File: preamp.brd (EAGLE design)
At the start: 100 x 80 mm, 70 parts, among them IC1 INA217DW, IC2 OPA134U, IC3 PCM1808, IC4 12.288MHz, IC5 REG1117

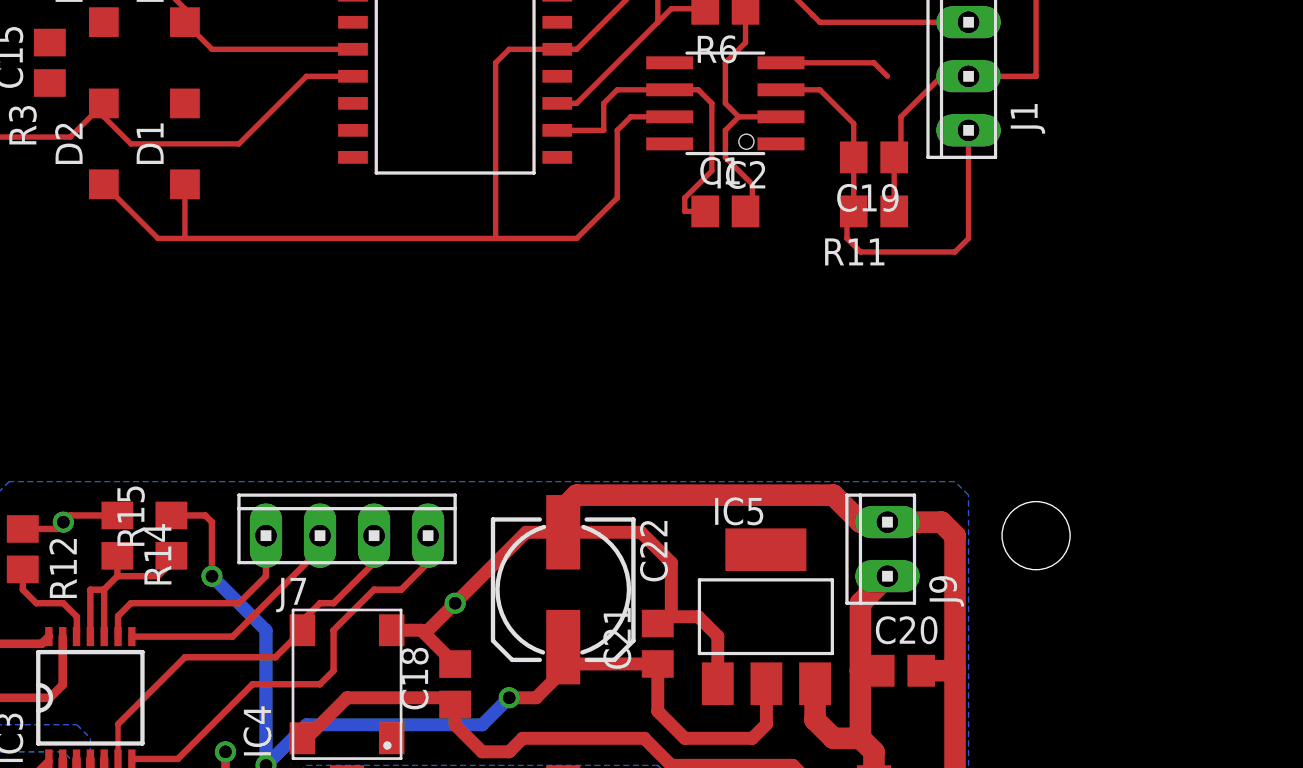
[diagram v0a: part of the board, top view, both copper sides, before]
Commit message: after review: named wires, add divider to ref voltage, add GND to digital pins
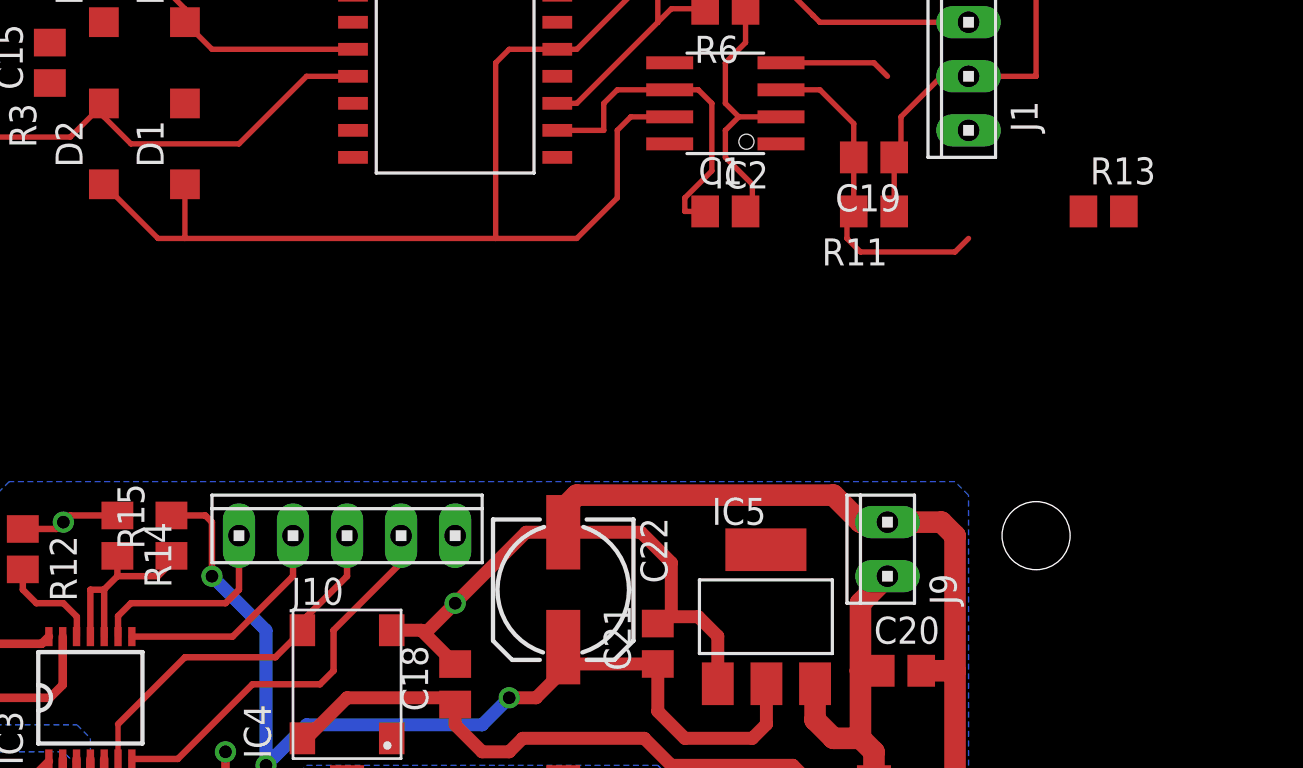
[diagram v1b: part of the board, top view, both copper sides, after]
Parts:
- removed J7: (no value), con-amp:10X04MTA
- added J10: (no value), con-amp:10X05MTA
- added R13: 0, rcl:R0805
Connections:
- new net N$28: J1.3, R13.2
- net GND: now also J10.1
- net N$15: now also R13.1; no longer J1.3
- net N$18: now also J10.2; no longer J7.1
- net N$19: now also J10.4; no longer J7.3
- net N$8: now also J10.3; no longer J7.2
- net N$9: now also J10.5; no longer J7.4
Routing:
- net N$15: track 20.9 -> 15.8 mm
- net N$18: track 20.1 -> 18.9 mm
- net N$9: track 10.6 -> 9.70 mm
- net N$8: track 18.8 -> 17.9 mm
- net N$19: track 11.2 -> 10.7 mm
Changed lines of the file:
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@@
 <element name="IC4" library="rpiadc" package="KXO-97" value="12.288MHz" x="40.005" y="14.605" rot="R90"/>
 <element name="C18" library="rcl" package="C0805" value="0.1" x="45.085" y="14.605" rot="R90"/>
-<element name="J7" library="con-amp" package="10X04MTA" value="" x="40.005" y="21.59"/>
 <element name="C19" library="rcl" package="C0805" value="0.1" x="64.77" y="39.37" rot="R180"/>
 <element name="R12" library="rcl" package="R0805" value="1k" x="24.765" y="20.955" rot="R270"/>
@@
 <element name="C31" library="rcl" package="153CLV-0605" value="47" x="40.005" y="6.35" rot="R90"/>
 <element name="R17" library="rcl" package="R0805" value="0" x="59.055" y="3.175"/>
+<element name="R13" library="rcl" package="R0805" value="0" x="75.565" y="36.83"/>
+<element name="J10" library="con-amp" package="10X05MTA" value="" x="40.005" y="21.59"/>
 </elements>
 <signals>
@@
 <contactref element="R11" pad="2"/>
 <contactref element="C19" pad="2"/>
-<contactref element="J1" pad="3"/>
-<wire x1="69.215" y1="40.64" x2="69.215" y2="35.56" width="0.254" layer="1"/>
 <wire x1="69.215" y1="35.56" x2="68.58" y2="34.925" width="0.254" layer="1"/>
 <wire x1="68.58" y1="34.925" x2="64.135" y2="34.925" width="0.254" layer="1"/>
@@
 <wire x1="63.82" y1="40.955" x2="62.23" y2="42.545" width="0.254" layer="1"/>
 <wire x1="62.23" y1="42.545" x2="60.4012" y2="42.545" width="0.254" layer="1"/>
+<contactref element="R13" pad="1"/>
+<wire x1="69.215" y1="35.56" x2="74.615" y2="36.83" width="0" layer="19" extent="1-1"/>
 </signal>
 <signal name="N$8">
@@
 <wire x1="29.24" y1="11.095" x2="29.24" y2="12.73" width="0.254" layer="1"/>
 <wire x1="37.905" y1="17.145" x2="37.905" y2="17.585" width="0.3048" layer="1"/>
-<contactref element="J7" pad="2"/>
 <wire x1="38.1" y1="17.78" x2="38.1" y2="17.34" width="0.3048" layer="1"/>
 <wire x1="38.1" y1="17.34" x2="37.905" y2="17.145" width="0.3048" layer="1"/>
@@
 <wire x1="32.385" y1="15.875" x2="36.635" y2="15.875" width="0.3048" layer="1"/>
 <wire x1="36.635" y1="15.875" x2="37.905" y2="17.145" width="0.3048" layer="1"/>
-<wire x1="41.275" y1="21.59" x2="41.275" y2="20.32" width="0.3048" layer="1"/>
-<wire x1="38.735" y1="18.415" x2="38.1" y2="17.78" width="0.3048" layer="1"/>
-<wire x1="38.735" y1="18.415" x2="39.37" y2="18.415" width="0.3048" layer="1"/>
-<wire x1="39.37" y1="18.415" x2="41.275" y2="20.32" width="0.3048" layer="1"/>
+<contactref element="J10" pad="3"/>
+<wire x1="38.1" y1="17.78" x2="40.005" y2="19.685" width="0.3048" layer="1"/>
+<wire x1="40.005" y1="19.685" x2="40.005" y2="21.59" width="0.3048" layer="1"/>
 </signal>
 <signal name="N$9">
@@
 <wire x1="29.24" y1="16.845" x2="29.24" y2="17.81" width="0.3048" layer="1"/>
 <wire x1="29.24" y1="17.81" x2="29.845" y2="18.415" width="0.3048" layer="1"/>
-<wire x1="29.845" y1="18.415" x2="34.925" y2="18.415" width="0.3048" layer="1"/>
-<contactref element="J7" pad="4"/>
-<wire x1="34.925" y1="18.415" x2="36.195" y2="19.685" width="0.3048" layer="1"/>
-<wire x1="36.195" y1="19.685" x2="36.195" y2="21.59" width="0.3048" layer="1"/>
+<contactref element="J10" pad="5"/>
+<wire x1="29.845" y1="18.415" x2="34.29" y2="18.415" width="0.3048" layer="1"/>
+<wire x1="34.29" y1="18.415" x2="34.925" y2="19.05" width="0.3048" layer="1"/>
+<wire x1="34.925" y1="19.05" x2="34.925" y2="21.59" width="0.3048" layer="1"/>
 </signal>
 <signal name="N$22">
@@
 <wire x1="50.8" y1="23.495" x2="50.165" y2="22.86" width="1.016" layer="1"/>
 <wire x1="50.165" y1="22.86" x2="50.165" y2="21.59" width="1.016" layer="1"/>
+<contactref element="J10" pad="1"/>
 <wire x1="11.11" y1="73.025" x2="10.795" y2="76.835" width="0" layer="19" extent="1-1"/>
 <wire x1="8.03" y1="67.865" x2="11.11" y2="73.025" width="0" layer="19" extent="1-1"/>
@@
 </signal>
 <signal name="N$18">
-<contactref element="J7" pad="1"/>
 <contactref element="IC3" pad="7"/>
 <wire x1="29.89" y1="11.095" x2="32.05" y2="11.095" width="0.3048" layer="1"/>
@@
 <wire x1="35.56" y1="14.605" x2="38.735" y2="14.605" width="0.3048" layer="1"/>
 <wire x1="38.735" y1="14.605" x2="39.37" y2="15.24" width="0.3048" layer="1"/>
-<wire x1="43.815" y1="21.59" x2="43.815" y2="20.32" width="0.3048" layer="1"/>
-<wire x1="43.815" y1="20.32" x2="42.545" y2="19.05" width="0.3048" layer="1"/>
-<wire x1="42.545" y1="19.05" x2="41.275" y2="19.05" width="0.3048" layer="1"/>
-<wire x1="41.275" y1="19.05" x2="39.37" y2="17.145" width="0.3048" layer="1"/>
+<wire x1="42.545" y1="20.32" x2="39.37" y2="17.145" width="0.3048" layer="1"/>
 <wire x1="39.37" y1="17.145" x2="39.37" y2="15.24" width="0.3048" layer="1"/>
+<contactref element="J10" pad="2"/>
+<wire x1="42.545" y1="20.32" x2="42.545" y2="21.59" width="0.3048" layer="1"/>
 </signal>
 <signal name="N$19">
 <contactref element="IC3" pad="8"/>
-<contactref element="J7" pad="3"/>
 <wire x1="29.89" y1="16.845" x2="34.625" y2="16.845" width="0.3048" layer="1"/>
-<wire x1="38.735" y1="21.59" x2="38.735" y2="20.955" width="0.3048" layer="1"/>
-<wire x1="38.735" y1="20.955" x2="34.625" y2="16.845" width="0.3048" layer="1"/>
+<contactref element="J10" pad="4"/>
+<wire x1="34.625" y1="16.845" x2="37.465" y2="19.685" width="0.3048" layer="1"/>
+<wire x1="37.465" y1="19.685" x2="37.465" y2="21.59" width="0.3048" layer="1"/>
 </signal>
 <signal name="N$26">
@@
 </polygon>
 </signal>
+<signal name="N$28">
+<contactref element="J1" pad="3"/>
+<contactref element="R13" pad="2"/>
+<wire x1="69.215" y1="40.64" x2="76.515" y2="36.83" width="0" layer="19" extent="1-1"/>
+</signal>
 </signals>

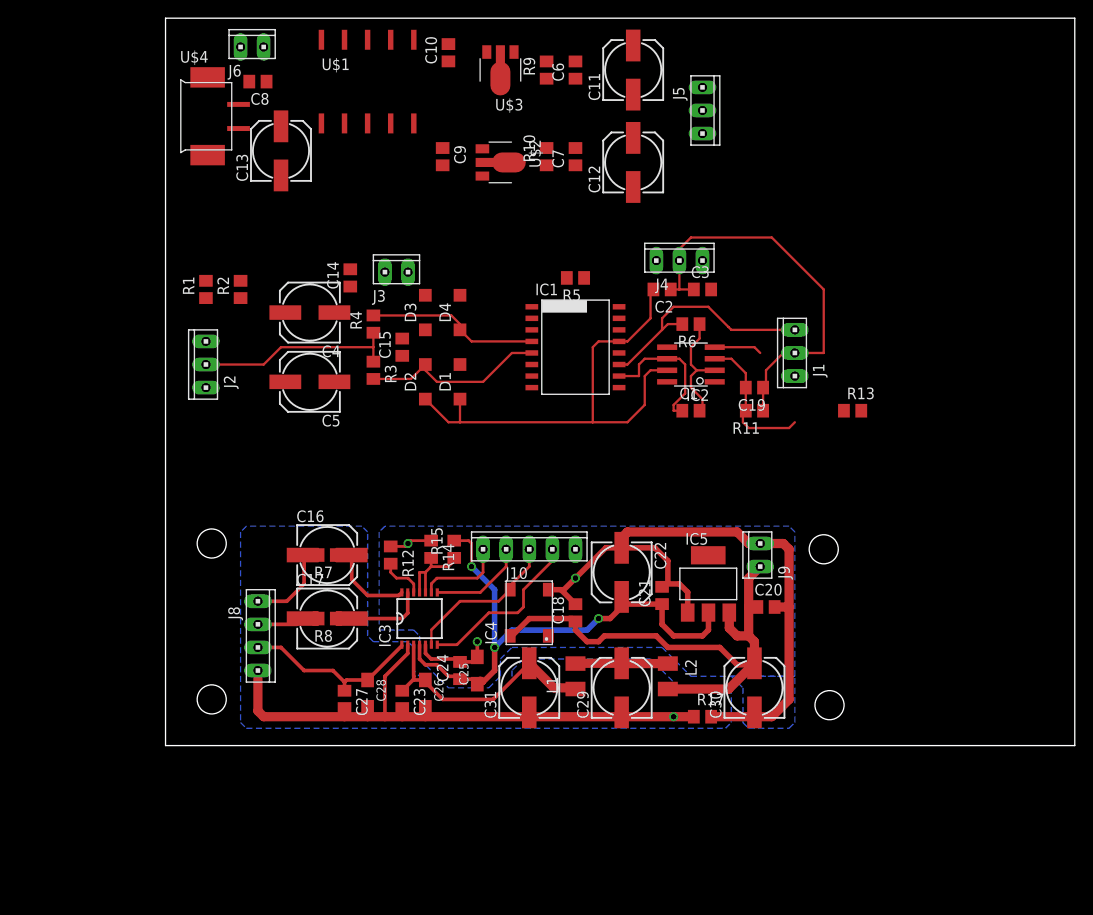
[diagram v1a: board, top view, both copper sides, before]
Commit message: route preamp, check DRC 0.254 mm
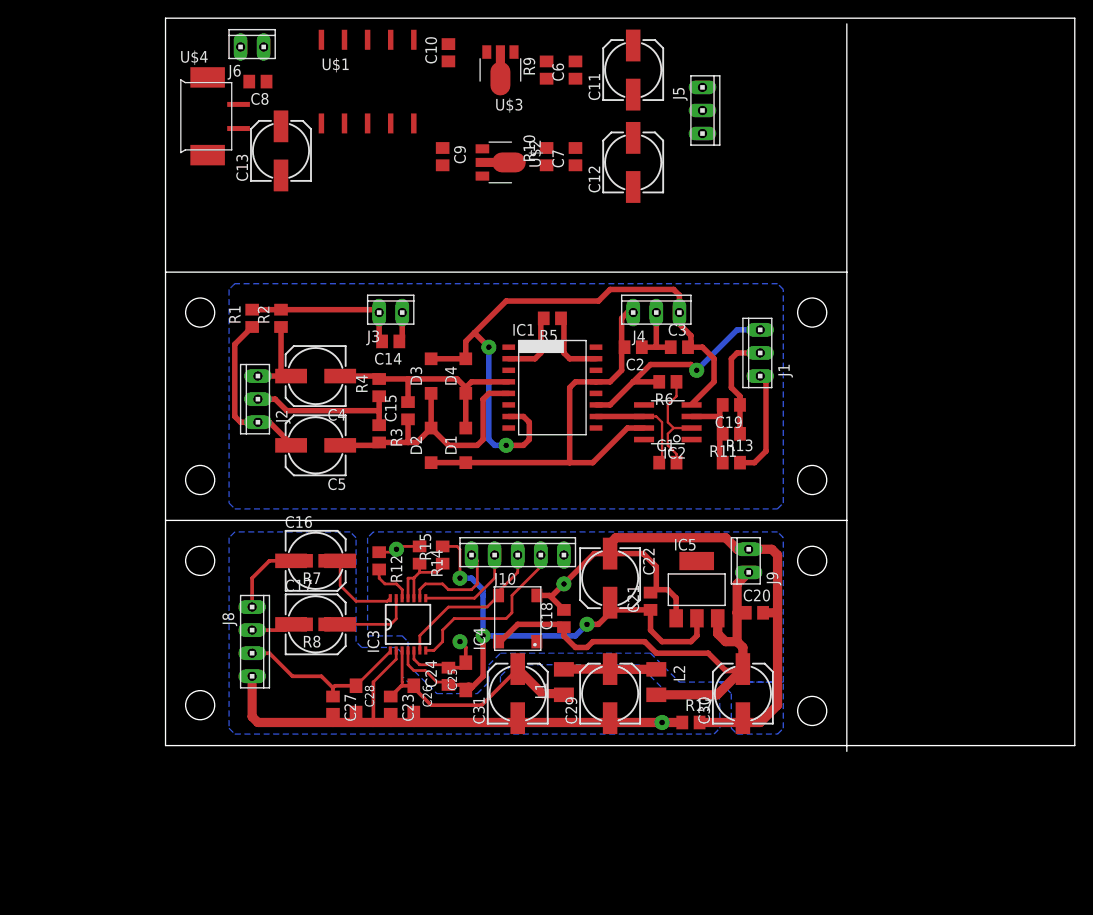
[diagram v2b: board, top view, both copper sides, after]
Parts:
- moved R13 14.5 mm to (62.2, 31.1)
- moved C14 8.28 mm to (24.8, 44.5), turned to 180 degrees
- moved C2 7.10 mm to (51.4, 43.8)
- moved C15 7.01 mm to (26.7, 36.8)
- moved C4 7.01 mm to (16.5, 40.6)
- moved C5 7.01 mm to (16.5, 33.0)
- moved D1 7.01 mm to (33.0, 33.0)
- moved D2 7.01 mm to (29.2, 33.0)
- moved D3 7.01 mm to (29.2, 40.6)
- moved D4 7.01 mm to (33.0, 40.6)
- moved R3 7.01 mm to (23.5, 34.3)
- moved R4 7.01 mm to (23.5, 39.4)
- moved J2 6.87 mm to (10.2, 38.1)
- moved C3 6.84 mm to (56.5, 43.8)
- moved IC2 6.84 mm to (55.2, 35.6)
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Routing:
- net V-: track 5.27 -> 69.5 mm, vias 0 -> 2
- net AGND: track 66.8 -> 39.4 mm
- net N$6: track 0.00 -> 18.2 mm
- net N$11: track 0.00 -> 17.4 mm
- net N$28: track 0.00 -> 11.9 mm
- net N$3: track 20.6 -> 31.6 mm
- net N$5: track 0.00 -> 9.05 mm
- net N$1: track 0.00 -> 7.74 mm
- net N$2: track 0.00 -> 7.74 mm
- net N$4: track 19.0 -> 26.5 mm
- net V+: track 53.6 -> 47.7 mm
- net N$15: track 15.8 -> 9.98 mm
- net N$14: track 15.6 -> 12.6 mm
- net N$9: track 9.70 -> 11.5 mm
- net N$13: track 26.2 -> 24.9 mm, vias 0 -> 1
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- added copper zone on layer 16, net AGND
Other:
- board size 100 x 80 mm -> 100 x 80.6 mm

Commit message: fix preamp dimentions, route power supply
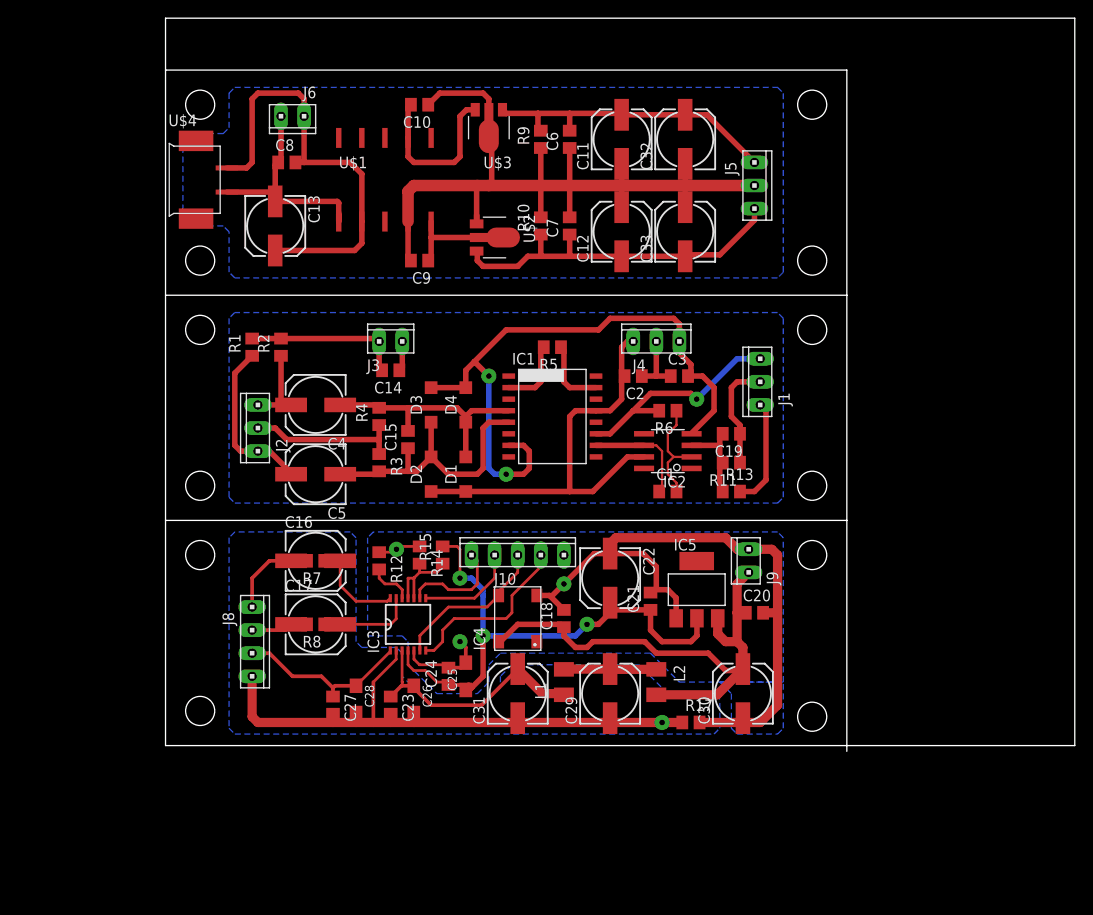
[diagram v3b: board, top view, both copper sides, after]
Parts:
- added C32, C33: 47, rcl:153CLV-0605
- moved C9 11.7 mm to (27.9, 53.3), turned to 180 degrees
- moved U$1 11.0 mm to (24.8, 62.2)
- moved J5 10.0 mm to (64.8, 61.6)
- moved C8 9.44 mm to (13.3, 64.1), turned to 0 degrees
- moved J6 8.82 mm to (14.0, 69.2), turned to 180 degrees
- moved C13 8.28 mm to (12.1, 57.1), turned to 270 degrees
- moved U$2 8.28 mm to (36.2, 55.9)
- moved C11 7.73 mm to (50.2, 66.7)
- moved C12 7.73 mm to (50.2, 56.5)
- moved C6 7.65 mm to (44.5, 66.7)
- moved R9 7.65 mm to (41.3, 66.7)
- moved C7 7.65 mm to (44.5, 57.1)
- moved R10 7.65 mm to (41.3, 57.1)
- moved U$4 7.10 mm to (3.81, 62.2)
- moved C10 6.54 mm to (27.9, 70.5), turned to 180 degrees
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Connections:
- net AGND: now also C32.-, C33.+
- net V+: now also C32.+
- net V-: now also C33.-
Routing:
- net AGND: track 39.4 -> 133.0 mm
- net VCC: track 60.7 -> 109.2 mm
- net V-: track 69.5 -> 109.5 mm
- net V+: track 47.7 -> 81.8 mm
- net GND: track 91.4 -> 116.8 mm
- net N$7: track 0.00 -> 18.5 mm
- net N$16: track 0.00 -> 9.68 mm
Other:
- outline, holes or cut-outs redrawn

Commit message: minor fixes in pcb
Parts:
- moved R5 0.64 mm to (42.5, 44.5)
- moved U$4 0.64 mm to (3.17, 62.2)
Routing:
- net V-: track 109.5 -> 112.8 mm
- net V+: track 81.8 -> 82.5 mm
- net N$1: track 7.74 -> 8.37 mm
- net VCC: track 109.2 -> 109.9 mm
- net N$2: track 7.74 -> 8.37 mm
- net GND: track 116.8 -> 117.4 mm
- net +3V3: track 63.1 -> 62.5 mm
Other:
- board size 100 x 80.6 mm -> 100 x 92.7 mm
